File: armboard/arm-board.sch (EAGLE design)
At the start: 49 parts, among them Q1 MOSFET-NCHANNELFDD8780, Q2 MOSFET-NCHANNELFDD8780, Q3 MOSFET-NCHANNELFDD8780

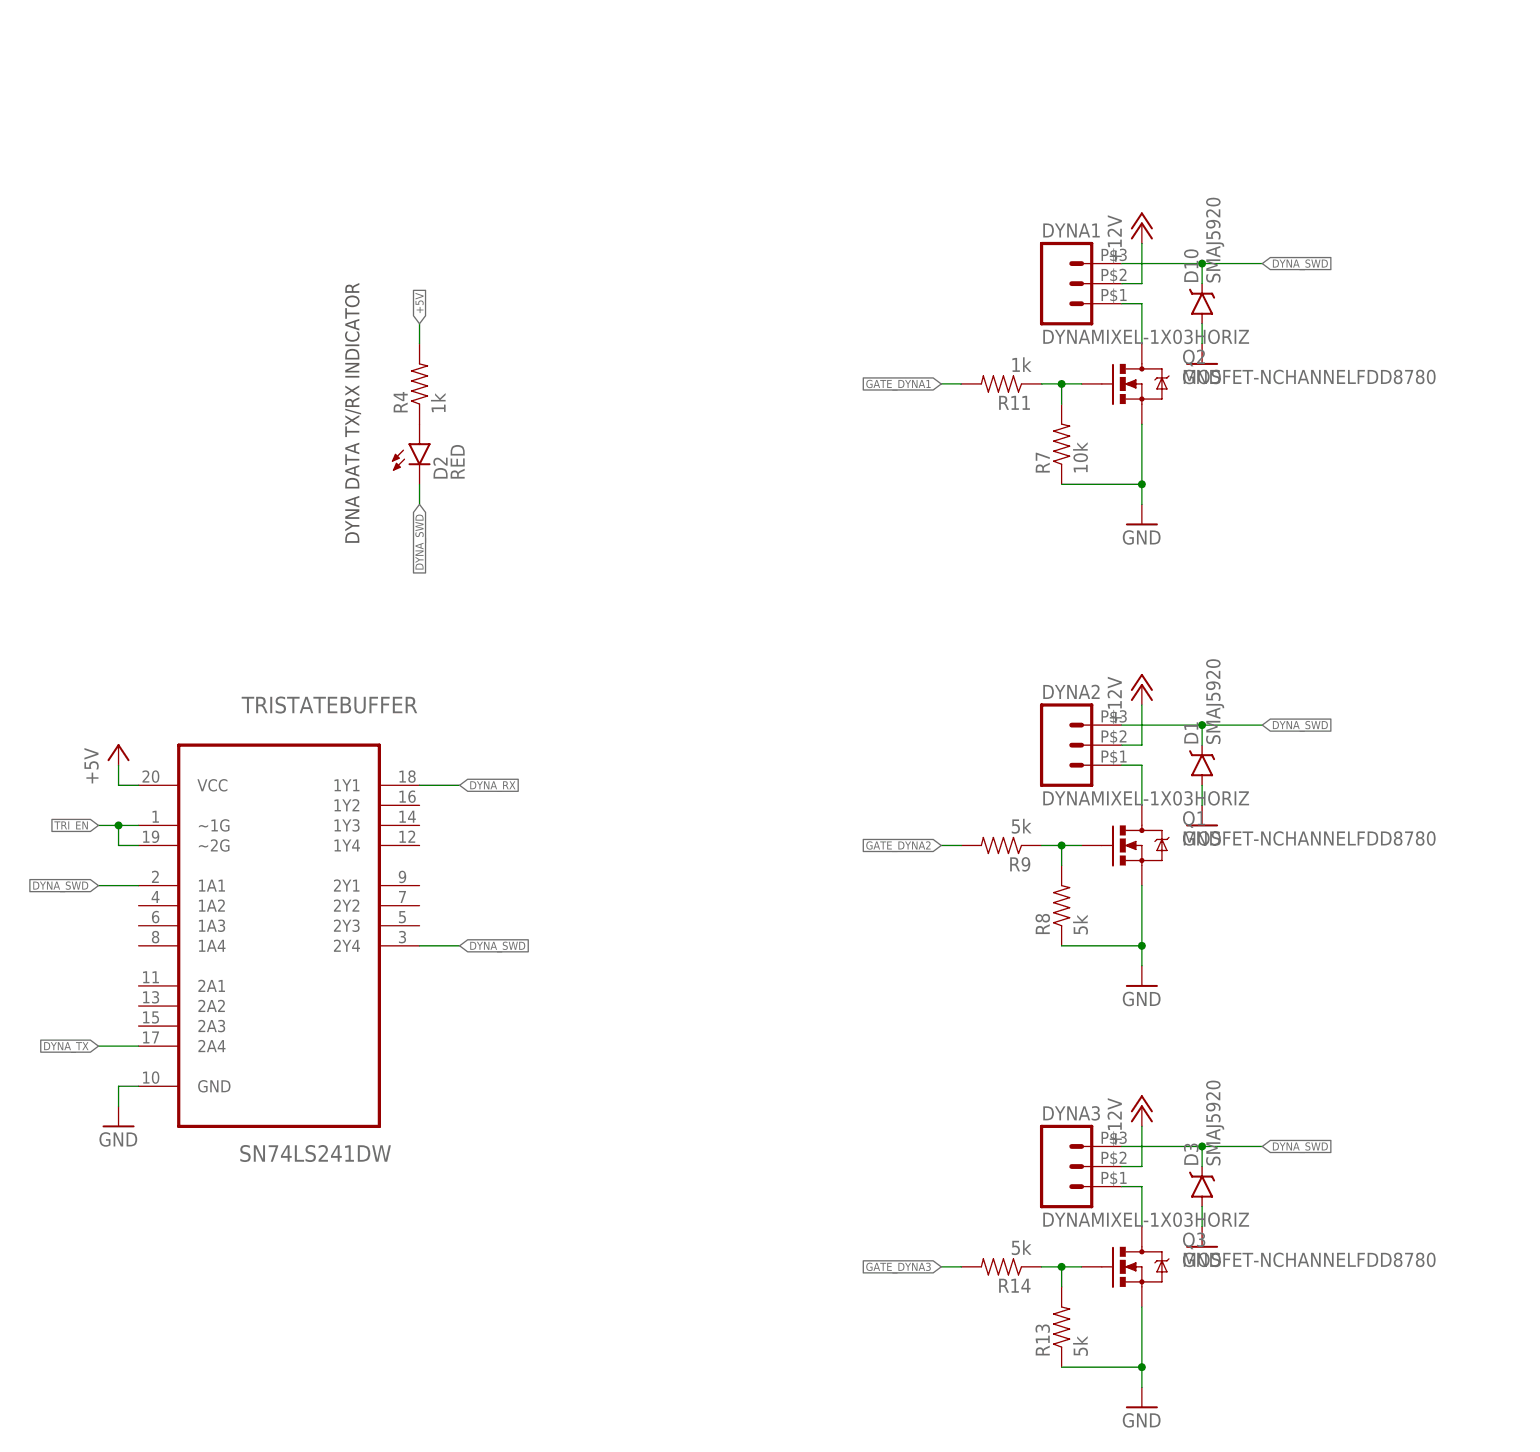
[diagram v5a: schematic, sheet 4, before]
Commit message: swap for all horiz conns, placement and routing
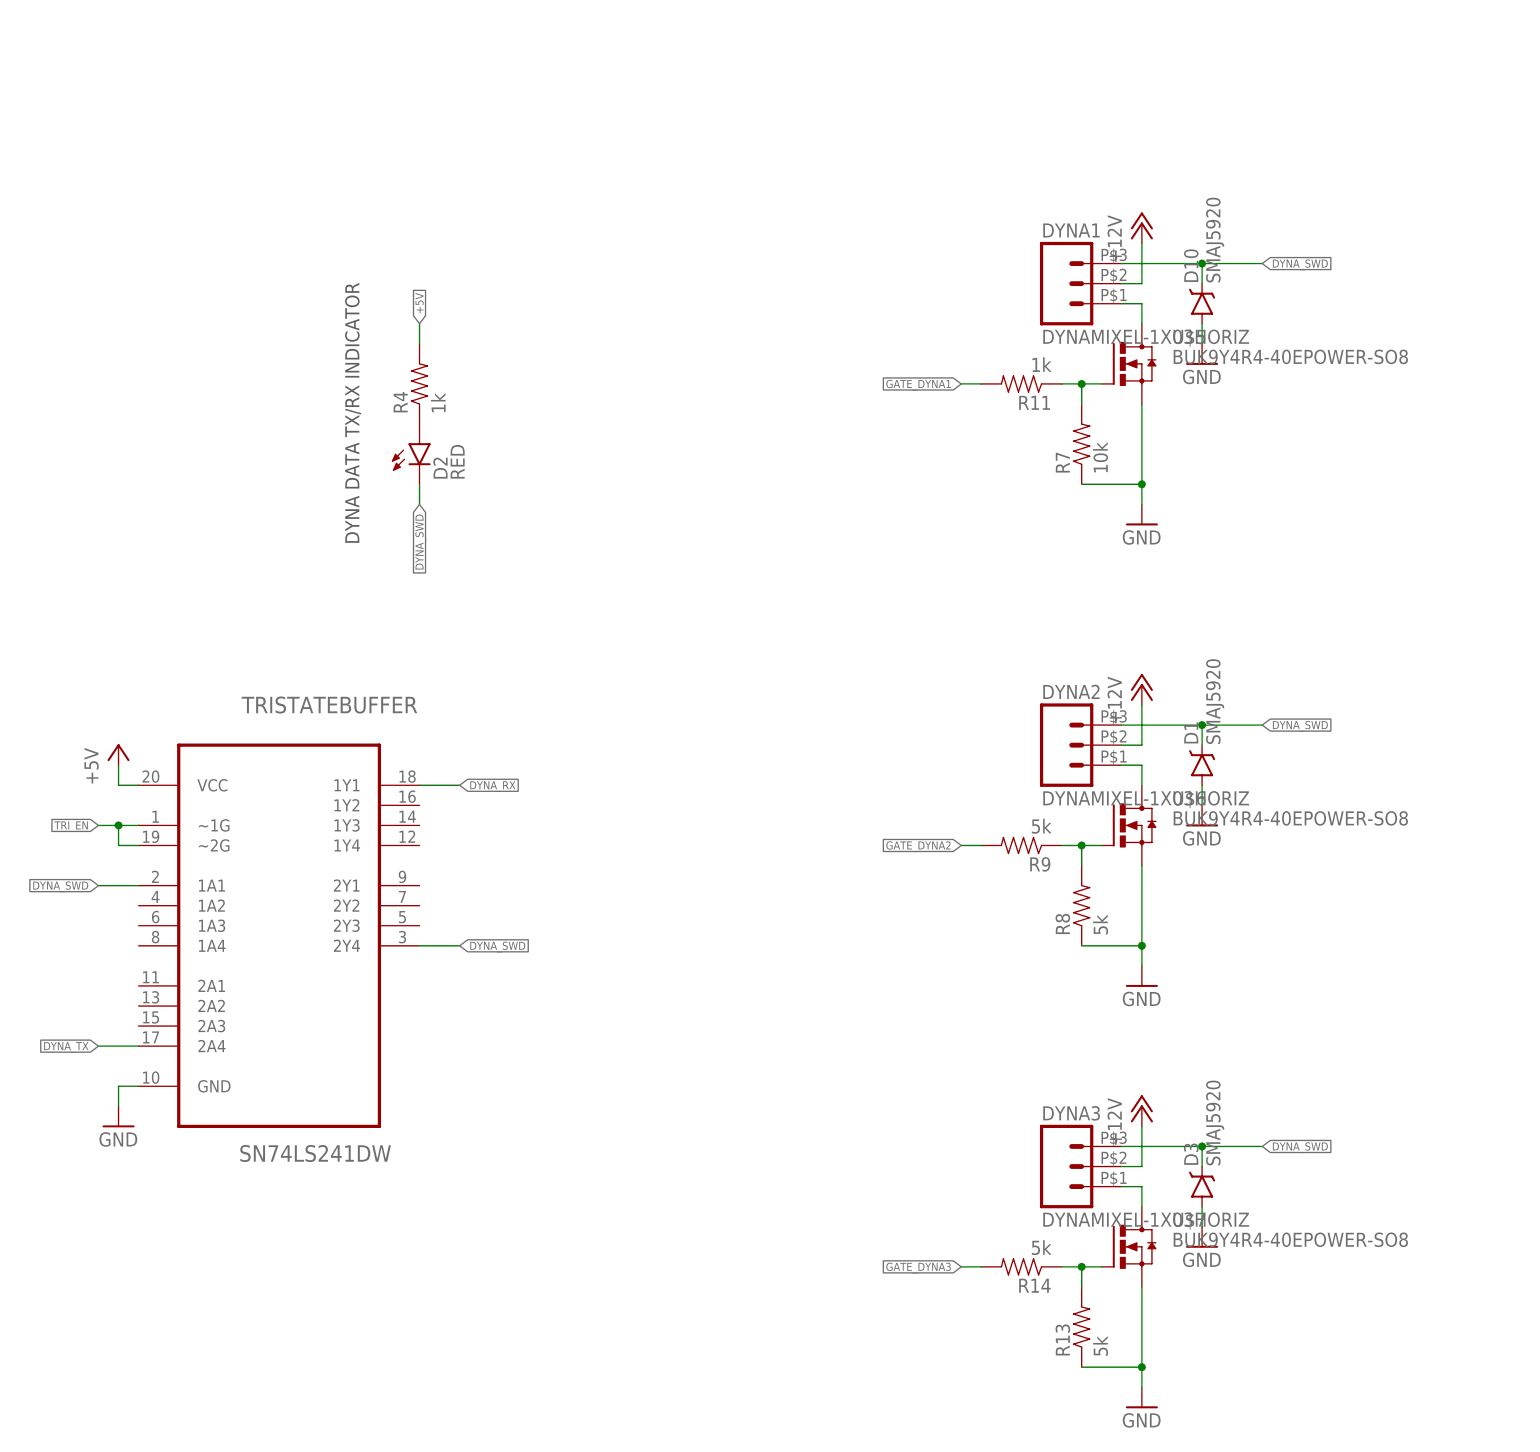
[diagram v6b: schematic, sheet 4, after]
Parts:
- removed CTRL_J2: 53047-06, con-molex:53047-06
- removed FET_EE1: IRF7910PBF, transistor-power:IRF7910PBF
- removed Q1, Q2, Q3: MOSFET-NCHANNELFDD8780, SparkFun-DiscreteSemi:MOSFET-NCHANNELFDD8780
- added U$2, U$3, U$5, U$6, U$7: BUK9Y4R4-40EPOWER-SO8, MRDT-2015-General:BUK9Y4R4-40EPOWER-SO8
- added X1: 53261-06, con-molex:53261-06
- ENC_EI, ENC_EO, ENC_J1, ENC_J2, ENC_WI, ENC_WO: value 53047-03 -> 53261-03; device con-molex:53047-03 -> con-molex:53261-03
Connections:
- net DYNA1_GND: now also U$5.D; no longer Q2.D
- net DYNA1_GND1: now also U$6.D; no longer Q1.D
- net DYNA1_GND2: now also U$7.D; no longer Q3.D
- net EE_GND1: now also U$3.D; no longer FET_EE1G$1.D
- net GND: now also U$2.S, U$3.S, U$5.S, U$6.S, U$7.S, X1-4.S; no longer CTRL_J2-4.S, FET_EE1G$1.S, FET_EE1G$2.S, Q1.S, Q3.S
- net J2_RC1: now also X1-3.S; no longer CTRL_J2-3.S
- net J2_TTLRX: now also X1-6.S; no longer CTRL_J2-6.S
- net J2_TTLTX: now also X1-5.S; no longer CTRL_J2-5.S
- net N$10: no longer Q1.G
- net N$11: now also U$3.G; no longer FET_EE1G$1.G
- net N$12: now also U$7.G; no longer Q3.G
- net N$6: now also U$5.G; no longer Q2.G
- net N$7: now also U$2.G; no longer FET_EE1G$2.G
- net R_OUT1: now also X1-2.S; no longer CTRL_J2-2.S
- net SOL_GND1: now also U$2.D; no longer FET_EE1G$2.D
- net T_OUT1: now also X1-1.S; no longer CTRL_J2-1.S
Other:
- moved on the sheet: R11, R13, R14, R7, R8, R9

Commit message: renamed some components
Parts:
- C10, C11, C8, C9: value 0.1uF -> 0.33uF
- C7: value 0.1uF -> .047uF
- renumbered C1 to DECAP, D1 to ZENER_DYNA2, D10 to ZENER_DYNA1, D2 to LED_DYNASWD, D3 to ZENER_DYNA3, R1 to RES_LEDPWR, R10 to RES_GATEPWRSOLPD, R11 to RES_GATEDYNA1, R12 to RES_GATEPWREE, R13 to RES_GATEDYNA3PD, R14 to RES_GATEDYNA3, R2 to RES_LEDXBRX, R3 to RES_LEDXBTX, R4 to RES_LEDDYNASWD, R5 to RES_GATEPWRSOL, R6 to RES_GATEPWREEPD, R7 to RES_GATEDYNA1PD, R8 to RES_GATEDYNA2PD, R9 to RES_GATEDYNA2, U$2 to FET_PWRSOL, U$3 to FET_PWREE, U$4 to MAX232, U$5 to FET_DYNA1, U$6 to FET_DYNA2, U$7 to FET_DYNA3
